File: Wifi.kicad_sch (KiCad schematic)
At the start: 8 parts, among them U2 ESP32-S3-MINI-1, U6 AMS1117-3.3

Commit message: added some lcsc part numbers
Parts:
- renumbered ESP to ESP1
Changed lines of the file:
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@@
 		(dnp no)
 		(fields_autoplaced yes)
-		(property "Reference" "ESP"
+		(property "Reference" "ESP1"
 			(at 30.48 20.32 0)
 			(show_name no)
@@
 			(project "TheDevBoard"
 				(path "/962e0ac6-7545-4a58-b6cb-cae1d23e787f/c6b54007-79c8-40fd-afa4-387886b604be"
-					(reference "ESP")
+					(reference "ESP1")
 					(unit 1)
 				)

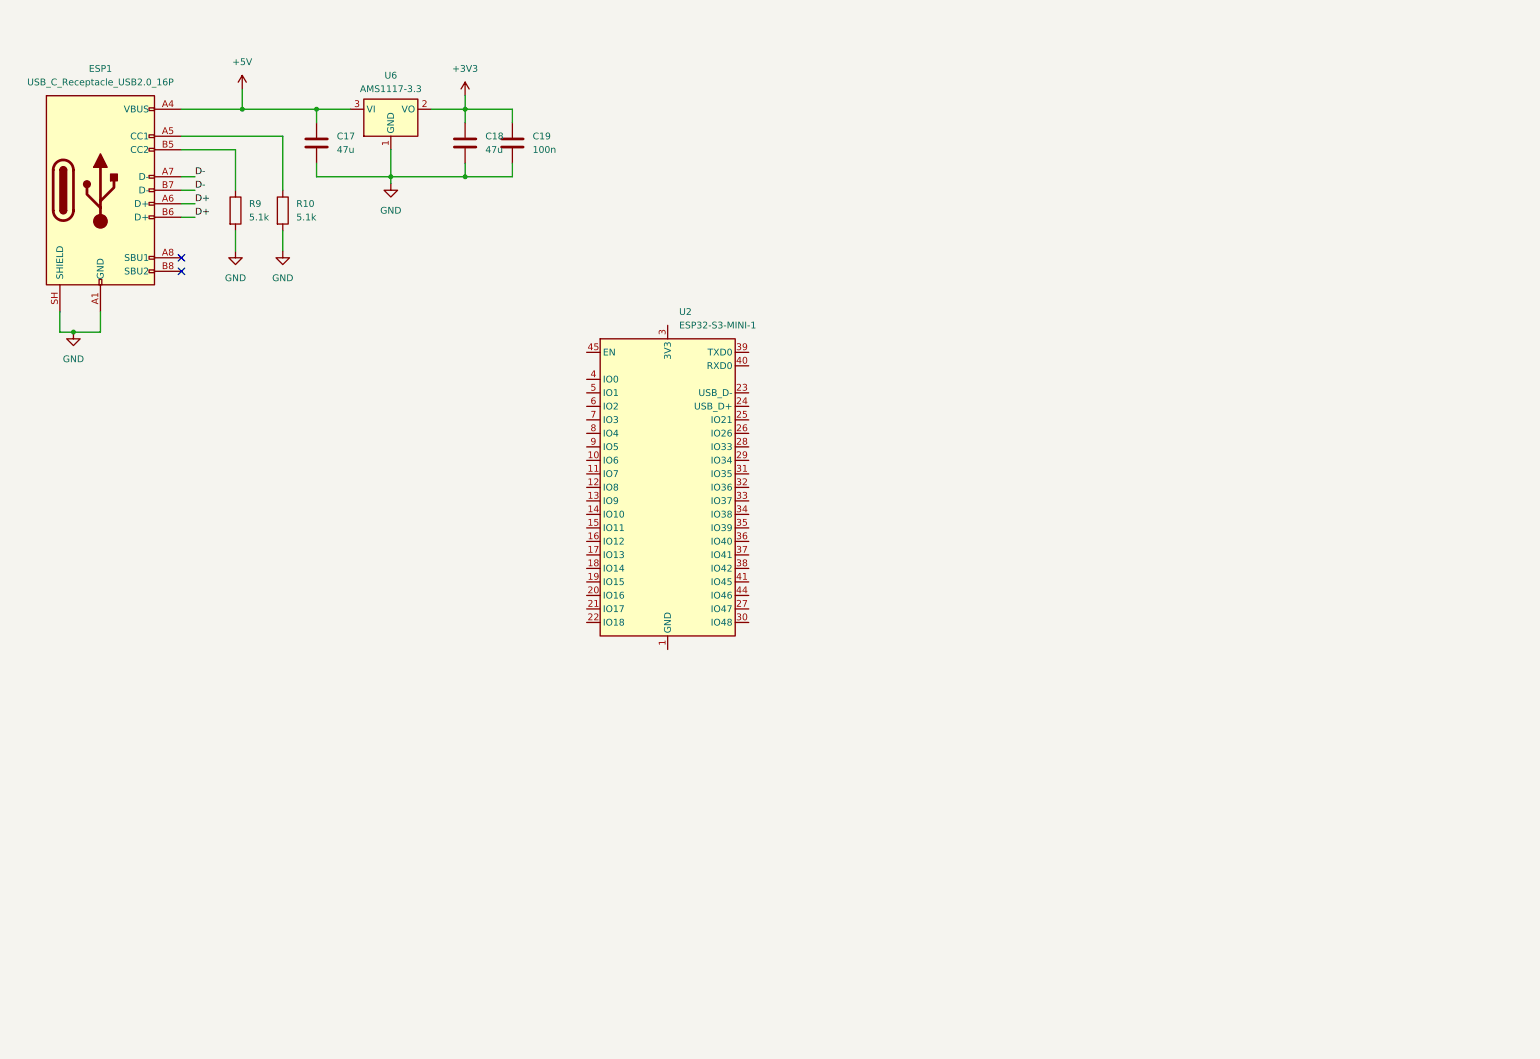
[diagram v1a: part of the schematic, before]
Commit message: created esp32 s3 mini connection to rp2350 added SD card Routed them together
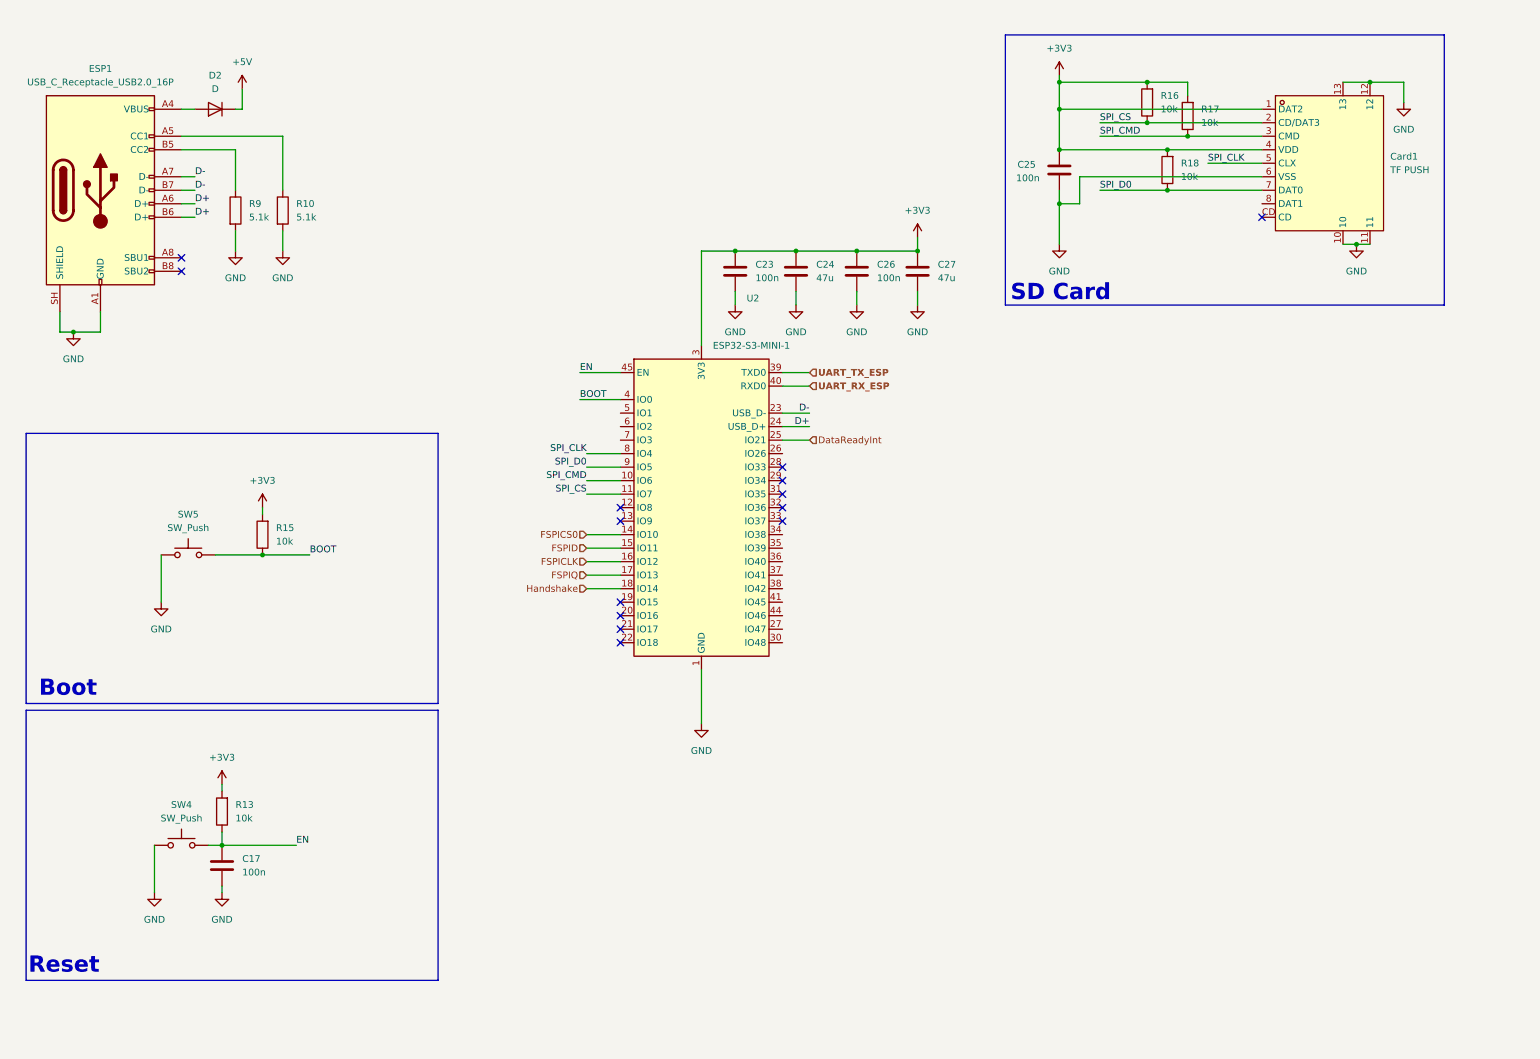
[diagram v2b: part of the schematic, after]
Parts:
- removed C18: 47u, Capacitor_SMD:C_0805_2012Metric_Pad1.18x1.45mm_HandSolder, symbol Device:C
- removed C19: 100n, Capacitor_SMD:C_0805_2012Metric_Pad1.18x1.45mm_HandSolder, symbol Device:C
- removed U6: AMS1117-3.3, Package_TO_SOT_SMD:SOT-223-3_TabPin2, symbol Regulator_Linear:AMS1117-3.3
- added C23, C25, C26: 100n, Capacitor_SMD:C_0805_2012Metric_Pad1.18x1.45mm_HandSolder, symbol Device:C
- added C24, C27: 47u, Capacitor_SMD:C_0805_2012Metric_Pad1.18x1.45mm_HandSolder, symbol Device:C
- added Card1: TF PUSH, EasyEDA:TF-SMD_TF-PUSH, symbol EasyEDA:TFPUSH
- added D2: D, Diode_SMD:D_0805_2012Metric, symbol Device:D
- added R13, R15, R16, R17, R18: 10k, Resistor_SMD:R_0805_2012Metric_Pad1.20x1.40mm_HandSolder, symbol Device:R
- added SW4, SW5: SW_Push, Button_Switch_SMD:SW_SPST_EVQPE1, symbol Switch:SW_Push
- C17: value 47u -> 100n
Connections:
- net +3V3: now also U2.3 (3V3), C23.1, C24.1, C25.1, C26.1, C27.1, Card1.1 (DAT2), Card1.4 (VDD), R13.2, R15.2, R16.2, R17.2, R18.2
- net +5V: now also D2.1 (K); no longer C17.1, ESP1.A4 (VBUS), ESP1.A9 (VBUS), ESP1.B4 (VBUS), ESP1.B9 (VBUS)
- net D+: now also U2.24 (USB_D+)
- net D-: now also U2.23 (USB_D-)
- net GND: now also U2.1 (GND), U2.2 (GND), U2.42 (GND), U2.43 (GND), U2.46 (GND), U2.47 (GND), U2.48 (GND), U2.49 (GND), U2.50 (GND), U2.51 (GND), U2.52 (GND), U2.53 (GND), U2.54 (GND), U2.55 (GND), U2.56 (GND), U2.57 (GND), U2.58 (GND), U2.59 (GND), U2.60 (GND), U2.61 (GND), U2.62 (GND), U2.63 (GND), U2.64 (GND), U2.65 (GND), C23.2, C24.2, C25.2, C26.2, C27.2, Card1.10, Card1.11, Card1.12, Card1.13, Card1.6 (VSS), SW4.1, SW5.1
- net SPI_CMD: now reaches U2.10 (IO6)
- net SPI_CMD: now also Card1.3 (CMD), R17.1
- net SPI_CS: now reaches U2.11 (IO7)
- net SPI_CS: now also Card1.2 (CD/DAT3), R16.1
- net FSPICS0: now reaches U2.14 (IO10)
- net FSPID: now reaches U2.15 (IO11)
- net FSPICLK: now reaches U2.16 (IO12)
- net FSPIQ: now reaches U2.17 (IO13)
- net Handshake: now reaches U2.18 (IO14)
- net DataReadyInt: now reaches U2.25 (IO21)
- net UART_TX_ESP: now reaches U2.39 (TXD0)
- net BOOT: now reaches U2.4 (IO0)
- net BOOT: now also R15.1, SW5.2
- net UART_RX_ESP: now reaches U2.40 (RXD0)
- net EN: now reaches U2.45 (EN)
- net EN: now also C17.1, R13.1, SW4.2
- net SPI_CLK: now reaches U2.8 (IO4)
- net SPI_CLK: now also Card1.5 (CLX)
- net SPI_D0: now reaches U2.9 (IO5)
- net SPI_D0: now also Card1.7 (DAT0), R18.1
- new net: D2.2 (A), ESP1.A4 (VBUS), ESP1.A9 (VBUS), ESP1.B4 (VBUS), ESP1.B9 (VBUS)
- no-connect marks 2 -> 14
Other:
- note added: "Boot"
- note added: "Reset"
- note added: "SD Card"
- moved on the sheet: U2
